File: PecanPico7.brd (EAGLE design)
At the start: 34.2 x 50 mm, 178 parts, among them IC1 Si4060-B1B-FM, IC10 TPS62260DRVT, IC11 TPS62261DRVT, IC12 TPS63021, IC13 RF6886, IC14 TPS78227DDCR, IC16 PAC1720-1-AIA-TR, IC2 Si4060-B1B-FM, IC3 BME280_BME280, IC4 uBlox MAX7/8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

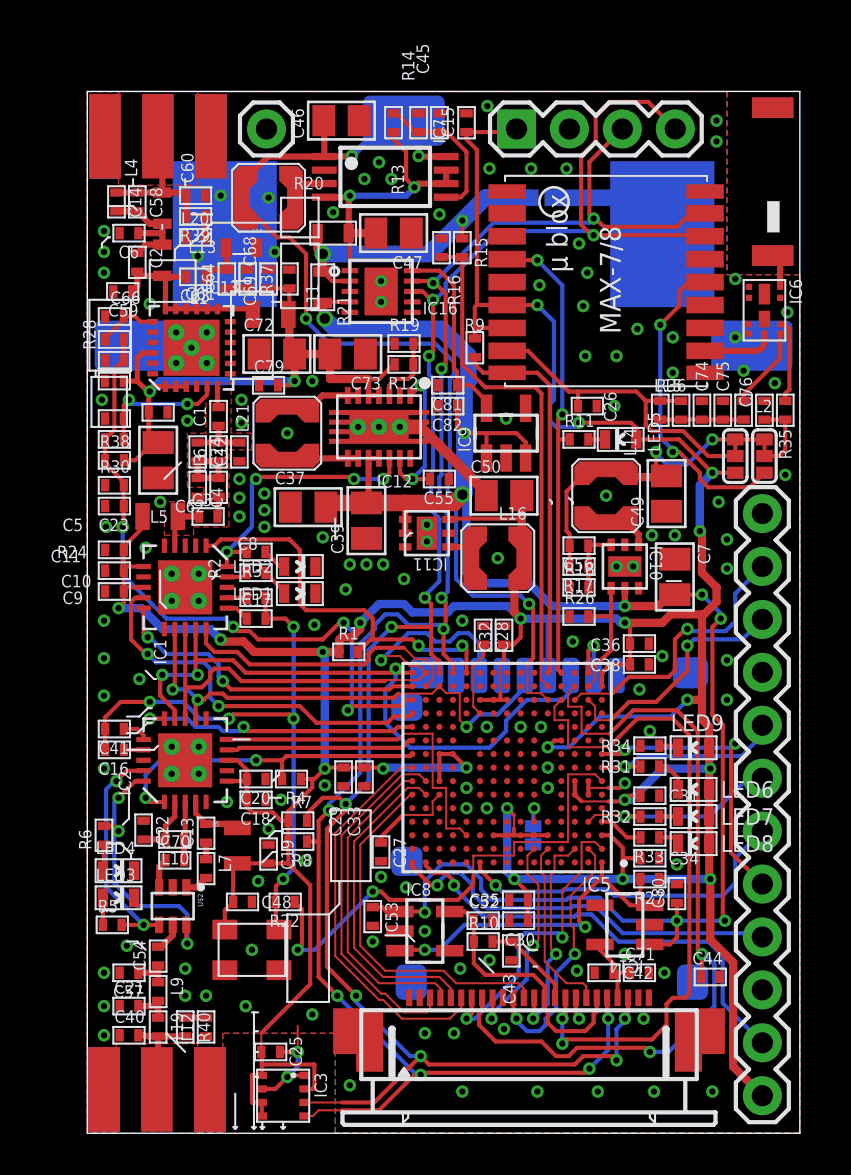
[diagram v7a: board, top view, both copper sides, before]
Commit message: Added decoupling capacitor
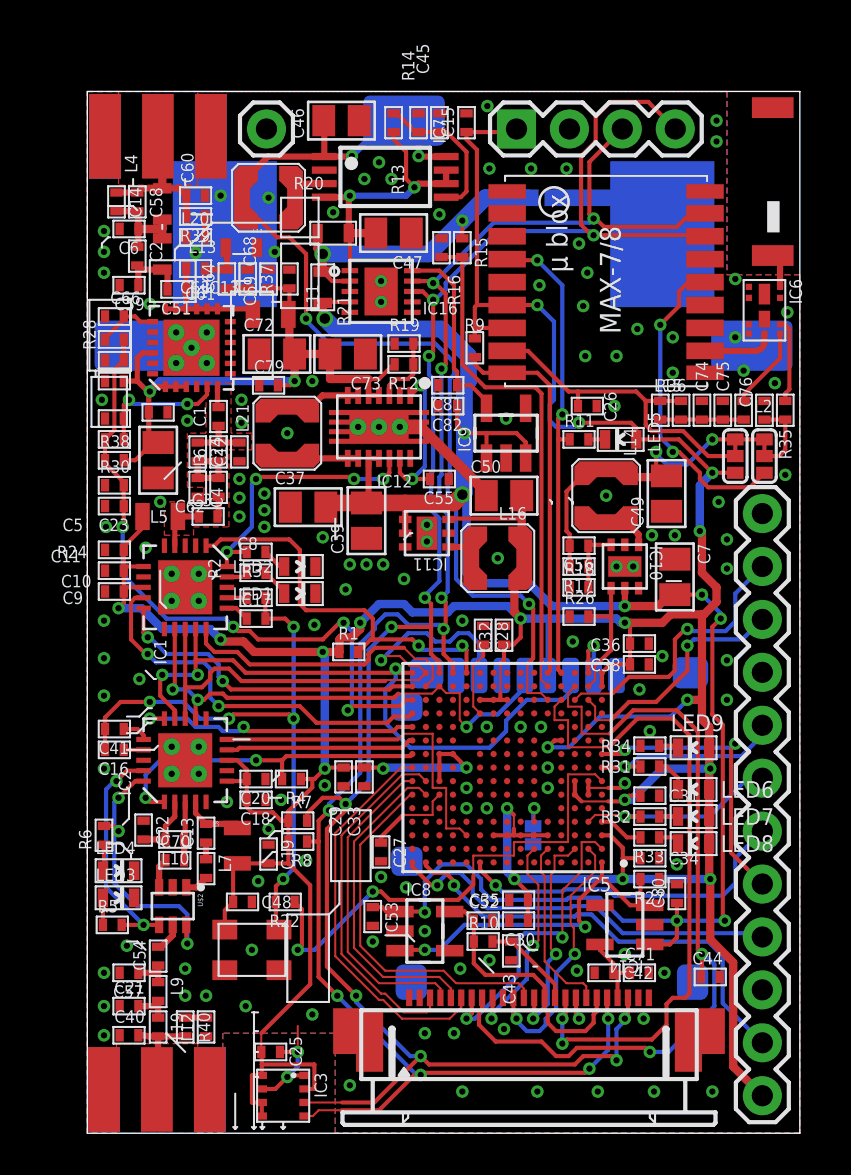
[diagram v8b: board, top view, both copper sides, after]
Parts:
- added C51: 470pF, PecanPico6:0402
- moved C59 0.42 mm to (2.00, 40.7)
- moved C63 0.40 mm to (5.20, 41.5)
- moved C2 0.30 mm to (2.40, 42.1)
- moved L1 0.30 mm to (3.60, 42.2)
- moved L4 0.20 mm to (3.60, 44.6)
- moved C6 0.20 mm to (2.00, 43.4)
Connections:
- new net N$8: C2.P$2, C51.P$2, C59.P$2, L1.P$1
- net N$43: now also C51.P$1; no longer C2.P$2, C59.P$2, L1.P$1
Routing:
- net N$8: track 0.00 -> 3.27 mm
- net N$43: track 9.47 -> 6.40 mm
- net N$5: track 5.96 -> 5.30 mm
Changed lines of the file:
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@@
 <attribute name="VALUE" x="6.5" y="30.3" size="0.6" layer="27" rot="R90"/>
 </element>
-<element name="C6" library="PecanPico6" package="0402" value="47pF" x="2" y="43.2" smashed="yes">
-<attribute name="NAME" x="1.5" y="42" size="0.6" layer="25"/>
-<attribute name="VALUE" x="1.3" y="42" size="0.6" layer="27"/>
+<element name="C6" library="PecanPico6" package="0402" value="47pF" x="2" y="43.4" smashed="yes">
+<attribute name="NAME" x="1.5" y="42.2" size="0.6" layer="25"/>
+<attribute name="VALUE" x="1.3" y="42.2" size="0.6" layer="27"/>
 </element>
 <element name="J$1" library="PecanPico4" package="SMA-EDGE" value="SMA_EDGE" x="0.85" y="47.85"/>
@@
 <attribute name="VALUE" x="7.5" y="33.7" size="0.6" layer="27" rot="R90"/>
 </element>
-<element name="C59" library="PecanPico6" package="0402" value="33pF" x="1.7" y="40.4" smashed="yes">
-<attribute name="NAME" x="1" y="39.2" size="0.6" layer="25"/>
-<attribute name="VALUE" x="1" y="39.2" size="0.6" layer="27"/>
+<element name="C59" library="PecanPico6" package="0402" value="33pF" x="2" y="40.7" smashed="yes">
+<attribute name="NAME" x="1.3" y="39.5" size="0.6" layer="25"/>
+<attribute name="VALUE" x="1.3" y="39.5" size="0.6" layer="27"/>
 </element>
 <element name="C60" library="PecanPico6" package="0402" value="30pF" x="5.2" y="45" smashed="yes" rot="R180">
@@
 <attribute name="VALUE" x="7.5" y="41.7" size="0.6" layer="27" rot="R270"/>
 </element>
-<element name="L1" library="sven2" package="0603@1" value="59nH" x="3.6" y="41.9" smashed="yes" rot="R90">
-<attribute name="NAME" x="5.8" y="40.4" size="0.6" layer="25" rot="R180"/>
-<attribute name="VALUE" x="4.8" y="40.9" size="0.2" layer="27" rot="R90"/>
-</element>
-<element name="L4" library="sven2" package="0603@1" value="51nH" x="3.6" y="44.4" smashed="yes" rot="R90">
-<attribute name="NAME" x="2.4" y="45.9" size="0.6" layer="25" rot="R90"/>
-<attribute name="VALUE" x="4.8" y="43.4" size="0.2" layer="27" rot="R90"/>
+<element name="L1" library="sven2" package="0603@1" value="59nH" x="3.6" y="42.2" smashed="yes" rot="R90">
+<attribute name="NAME" x="5.8" y="40.7" size="0.6" layer="25" rot="R180"/>
+<attribute name="VALUE" x="4.8" y="41.2" size="0.2" layer="27" rot="R90"/>
+</element>
+<element name="L4" library="sven2" package="0603@1" value="51nH" x="3.6" y="44.6" smashed="yes" rot="R90">
+<attribute name="NAME" x="2.4" y="46.1" size="0.6" layer="25" rot="R90"/>
+<attribute name="VALUE" x="4.8" y="43.6" size="0.2" layer="27" rot="R90"/>
 </element>
 <element name="L11" library="sven" package="0805@1" value="470nH" x="8.8" y="39.3" smashed="yes">
@@
 <element name="C54" library="PecanPico6" package="0402" value="470pF" x="3.4" y="8.5" rot="R90"/>
 <element name="C57" library="PecanPico6" package="0402" value="12pF" x="2" y="7.7" rot="R180"/>
-<element name="C2" library="PecanPico6" package="0402" value="2.2pF" x="2.4" y="41.8" rot="R270"/>
+<element name="C2" library="PecanPico6" package="0402" value="2.2pF" x="2.4" y="42.1" rot="R270"/>
 <element name="C58" library="PecanPico6" package="0402" value="3.3pF" x="2.4" y="44.7" rot="R270"/>
-<element name="C63" library="PecanPico6" package="0402" value="8.2pF" x="5.2" y="41.1" rot="R180"/>
+<element name="C63" library="PecanPico6" package="0402" value="8.2pF" x="5.2" y="41.5" rot="R180"/>
 <element name="C64" library="PecanPico6" package="0402" value="8.2pF" x="6.7" y="41" rot="R90"/>
 <element name="R37" library="PecanPico6" package="0402" value="51R" x="7.7" y="41" rot="R270"/>
@@
 <element name="R10" library="PecanPico6" package="0402" value="DIODE" x="19" y="9.2"/>
 <element name="R22" library="PecanPico6" package="0402" value="10k" x="9.5" y="11.1" rot="R180"/>
+<element name="C51" library="PecanPico6" package="0402" value="470pF" x="4.3" y="40.5" rot="R180"/>
 </elements>
 <signals>
@@
 <via x="9.6" y="33.6" extent="1-16" drill="0.3"/>
 <via x="10.8" y="36.1" extent="1-16" drill="0.3"/>
-<via x="5.3" y="42.1" extent="1-16" drill="0.3"/>
+<via x="5.2" y="42.25" extent="1-16" drill="0.3"/>
 <via x="8.7" y="44.9" extent="1-16" drill="0.3"/>
 <via x="25.3" y="34.9" extent="1-16" drill="0.3"/>
@@
 <via x="15.3" y="11.8" extent="1-16" drill="0.3"/>
 <via x="17.9" y="7.9" extent="1-16" drill="0.3"/>
-<polygon width="0.1" layer="1">
-<vertex x="15.1" y="22.6"/>
-<vertex x="25.2" y="22.6"/>
-<vertex x="25.2" y="13.1"/>
-<vertex x="25.2" y="12.5"/>
-<vertex x="15.5" y="12.5"/>
-<vertex x="15.1" y="12.5"/>
-</polygon>
 <via x="3" y="39.8" extent="1-16" drill="0.3"/>
 <wire x1="19.45" y1="10.2" x2="19.3" y2="8.3" width="0" layer="19" extent="1-1"/>
@@
 <contactref element="C58" pad="P$2"/>
 <contactref element="C14" pad="P$2"/>
-<wire x1="3.6" y1="42.65" x2="3.6" y2="43.2" width="0.3" layer="1"/>
 <wire x1="1.4" y1="44.25" x2="2.4" y2="44.25" width="0.3" layer="1"/>
-<wire x1="2.4" y1="44.25" x2="3" y2="43.65" width="0.3" layer="1"/>
-<wire x1="3" y1="43.65" x2="3.6" y2="43.65" width="0.3" layer="1"/>
-<wire x1="2.4" y1="42.25" x2="2.8" y2="42.65" width="0.3" layer="1"/>
-<wire x1="2.8" y1="42.65" x2="3.6" y2="42.65" width="0.3" layer="1"/>
-<wire x1="2.45" y1="43.2" x2="3.6" y2="43.2" width="0.3" layer="1"/>
-<wire x1="3.6" y1="43.2" x2="3.6" y2="43.65" width="0.3" layer="1"/>
+<wire x1="2.4" y1="42.55" x2="2.45" y2="42.55" width="0.3" layer="1"/>
+<wire x1="2.45" y1="42.55" x2="2.45" y2="43.4" width="0.3" layer="1"/>
+<wire x1="3.6" y1="42.95" x2="3.6" y2="43.85" width="0.4" layer="1"/>
+<wire x1="2.45" y1="43.4" x2="3.6" y2="43.4" width="0.4" layer="1"/>
+<wire x1="3.6" y1="43.4" x2="3.6" y2="43.85" width="0.4" layer="1"/>
+<wire x1="2.4" y1="44.25" x2="2.45" y2="44.25" width="0.3" layer="1"/>
+<wire x1="2.45" y1="44.25" x2="2.45" y2="43.4" width="0.3" layer="1"/>
 </signal>
 <signal name="CLOCK">
@@
 <contactref element="C14" pad="P$1"/>
 <wire x1="1.4" y1="45.15" x2="2.4" y2="45.15" width="0.3" layer="1"/>
-<wire x1="3.6" y1="45.15" x2="4.6" y2="45.15" width="0.3" layer="1"/>
-<wire x1="4.6" y1="45.15" x2="4.75" y2="45" width="0.3" layer="1"/>
 <wire x1="4.75" y1="45" x2="4.75" y2="44" width="0.3" layer="1"/>
-<wire x1="3.39" y1="47.85" x2="3.6" y2="47.85" width="0.3" layer="1"/>
-<wire x1="3.6" y1="47.85" x2="3.6" y2="45.15" width="0.3" layer="1"/>
-<wire x1="3.6" y1="45.15" x2="2.4" y2="45.15" width="0.3" layer="1"/>
+<wire x1="3.6" y1="45.35" x2="3.6" y2="47.85" width="0.4" layer="1"/>
+<wire x1="3.6" y1="47.85" x2="3.39" y2="47.85" width="0.4" layer="1"/>
+<wire x1="2.4" y1="45.15" x2="2.6" y2="45.35" width="0.3" layer="1"/>
+<wire x1="2.6" y1="45.35" x2="3.6" y2="45.35" width="0.3" layer="1"/>
+<wire x1="3.6" y1="45.35" x2="4.4" y2="45.35" width="0.3" layer="1"/>
+<wire x1="4.4" y1="45.35" x2="4.75" y2="45" width="0.3" layer="1"/>
 </signal>
 <signal name="RADIO1_VREG2">
@@
 <contactref element="IC13" pad="18"/>
 <contactref element="L11" pad="P$1"/>
-<contactref element="C2" pad="P$2"/>
-<contactref element="L1" pad="P$1"/>
-<contactref element="C59" pad="P$2"/>
 <contactref element="C63" pad="P$2"/>
 <wire x1="3.75" y1="39.564" x2="4.25" y2="39.564" width="0.25" layer="1"/>
@@
 <wire x1="5.25" y1="39.564" x2="5.75" y2="39.564" width="0.25" layer="1"/>
 <wire x1="5.75" y1="39.564" x2="6.25" y2="39.564" width="0.25" layer="1"/>
-<wire x1="2.15" y1="40.4" x2="2.4" y2="40.65" width="0.3" layer="1"/>
-<wire x1="2.4" y1="40.65" x2="2.4" y2="41.15" width="0.3" layer="1"/>
-<wire x1="3.6" y1="41.15" x2="2.4" y2="41.15" width="0.3" layer="1"/>
-<wire x1="2.4" y1="41.15" x2="2.4" y2="41.35" width="0.3" layer="1"/>
-<wire x1="3.6" y1="41.15" x2="3.75" y2="41.15" width="0.25" layer="1"/>
-<wire x1="3.75" y1="41.15" x2="3.75" y2="39.564" width="0.25" layer="1"/>
-<wire x1="3.75" y1="41.15" x2="3.8" y2="41.1" width="0.3" layer="1"/>
-<wire x1="3.8" y1="41.1" x2="4.75" y2="41.1" width="0.3" layer="1"/>
 <wire x1="6.25" y1="39.564" x2="7.95" y2="39.564" width="0.25" layer="1"/>
 <wire x1="7.95" y1="39.564" x2="7.95" y2="39.3" width="0.25" layer="1"/>
+<contactref element="C51" pad="P$1"/>
+<wire x1="4.75" y1="40.5" x2="4.75" y2="39.564" width="0.25" layer="1"/>
+<wire x1="4.75" y1="40.5" x2="4.75" y2="41.5" width="0.25" layer="1"/>
 </signal>
 <signal name="SD_CS">
@@
 <contactref element="C63" pad="P$1"/>
 <contactref element="L17" pad="P$2"/>
-<wire x1="5.65" y1="41.1" x2="6" y2="41.45" width="0.3" layer="1"/>
-<wire x1="6" y1="41.45" x2="6.7" y2="41.45" width="0.3" layer="1"/>
 <wire x1="6.7" y1="41.45" x2="6.7" y2="42.5" width="0.3" layer="1"/>
 <wire x1="6.7" y1="42.5" x2="6.65" y2="42.5" width="0.3" layer="1"/>
+<wire x1="5.65" y1="41.5" x2="5.65" y2="41.45" width="0.3" layer="1"/>
+<wire x1="5.65" y1="41.45" x2="6.7" y2="41.45" width="0.3" layer="1"/>
 </signal>
 <signal name="N$24">
@@
 <wire x1="20.35" y1="9.2" x2="19.45" y2="9.2" width="0.2" layer="1"/>
 </signal>
+<signal name="N$8">
+<contactref element="C59" pad="P$2"/>
+<contactref element="C2" pad="P$2"/>
+<contactref element="L1" pad="P$1"/>
+<contactref element="C51" pad="P$2"/>
+<wire x1="3.6" y1="41.45" x2="3.85" y2="41.35" width="0.3" layer="1"/>
+<wire x1="3.85" y1="41.35" x2="3.85" y2="40.5" width="0.3" layer="1"/>
+<wire x1="2.4" y1="41.65" x2="2.45" y2="41.65" width="0.3" layer="1"/>
+<wire x1="2.45" y1="41.65" x2="2.45" y2="41.45" width="0.3" layer="1"/>
+<wire x1="3.6" y1="41.45" x2="2.45" y2="41.45" width="0.3" layer="1"/>
+<wire x1="2.45" y1="41.45" x2="2.45" y2="40.7" width="0.3" layer="1"/>
+</signal>
 </signals>
